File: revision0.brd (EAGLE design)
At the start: 99.5 x 80 mm, 102 parts, among them IC1 MSP430FR698X(1)80-PIN_PN, IC3 FT232RL

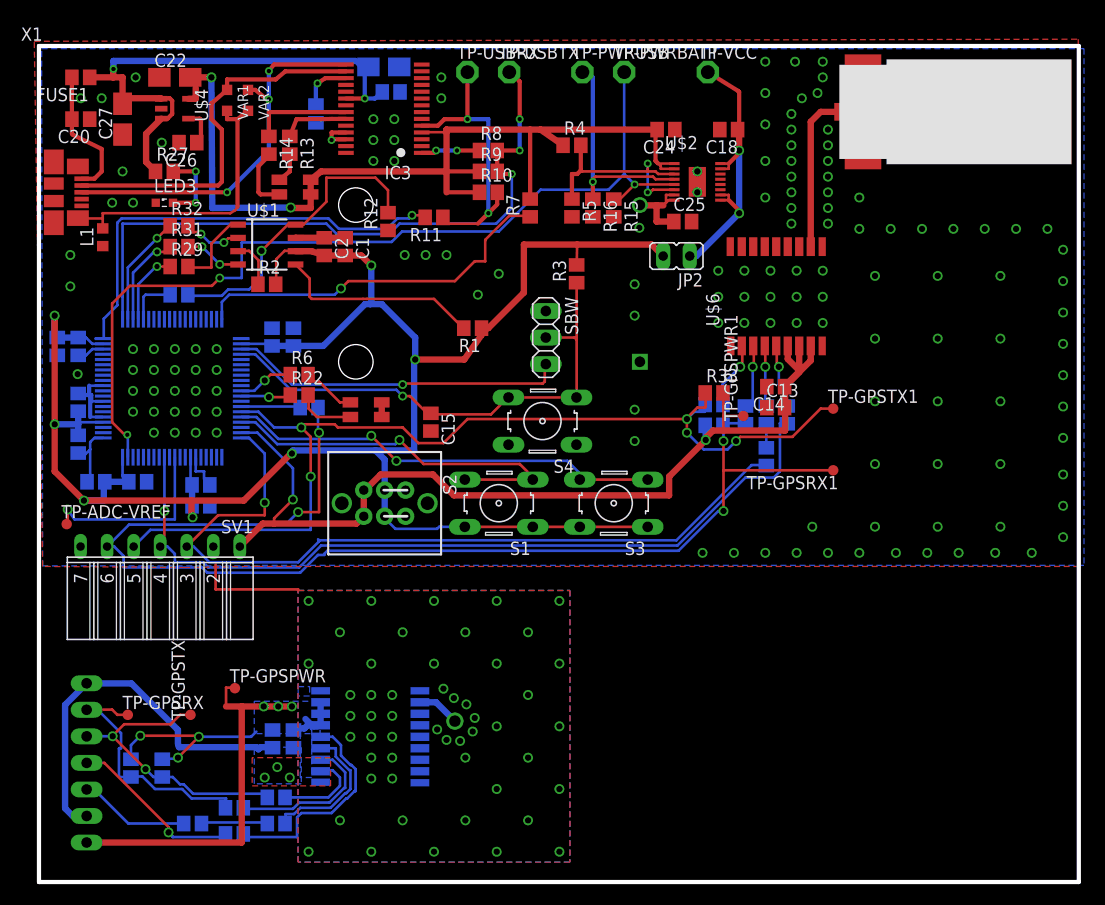
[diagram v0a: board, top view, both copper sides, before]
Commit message: Add ceramic antenna, move the patch antenna connetor a bit
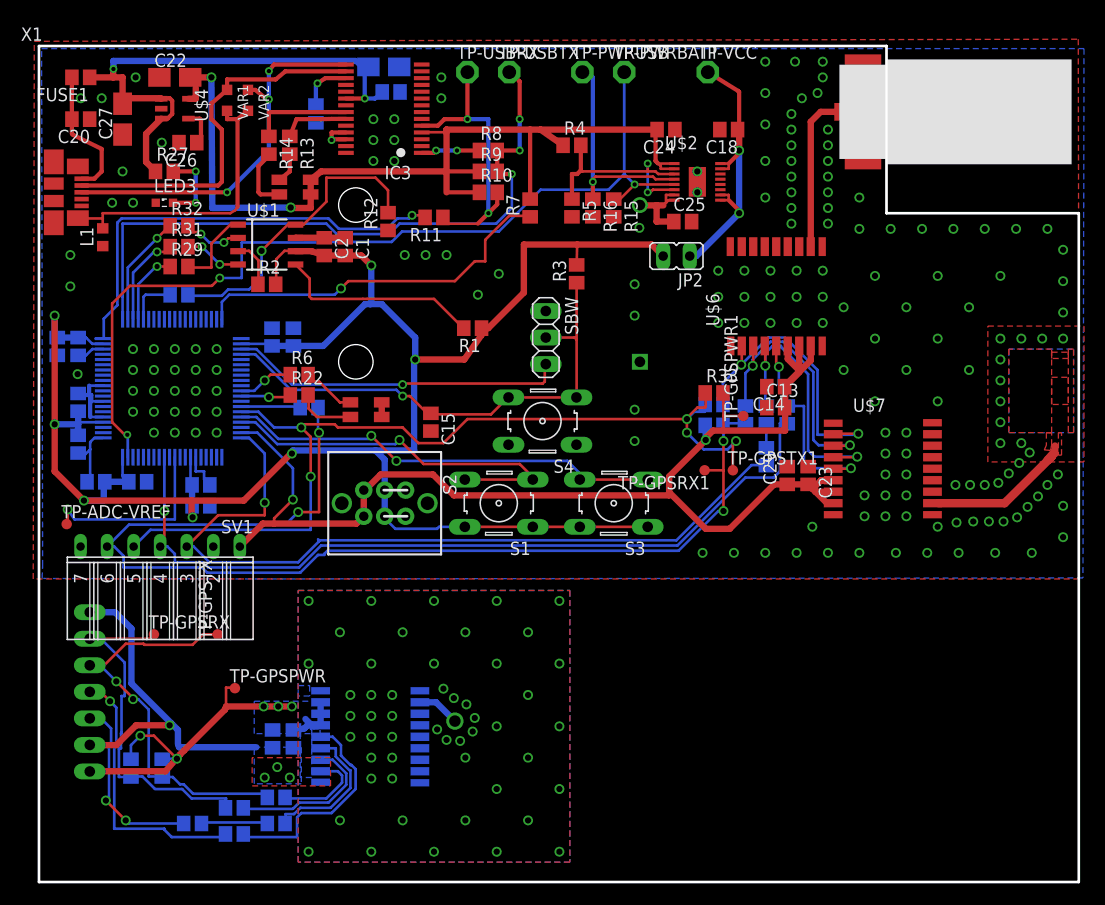
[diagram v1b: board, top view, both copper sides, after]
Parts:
- added C23: 100n, tagps:C0805
- added C29: 1u, tagps:C0805
- added U$7: MAX-8C-0, tagps:MAX-8
- moved TP-GPSRX1 12.3 mm to (63.7, 39.4)
- moved TP-GPSTX1 11.3 mm to (66.4, 39.4)
- moved TP-GPSTX 8.13 mm to (17.1, 23.7)
- moved TP-GPSRX 8.10 mm to (11.0, 23.7)
- moved JP1 6.81 mm to (1.05, 18.2)
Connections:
- removed net N$48: FB4.1, U$6.3
- new net N$15: FB4.1, U$6.3, U$7.3
- net GND: now also C23.1, C29.2, U$7.1, U$7.10, U$7.12
- net MB-PWR_GPS_SENSE: now also C23.2, C29.1, U$7.6, U$7.7, U$7.8
- net N$46: now also U$7.5
- net N$49: now also U$7.2
- net N$50: now also U$7.4
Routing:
- net N$15: track 0.00 -> 26.2 mm, vias 0 -> 2
- net MB-PWR_GPS_SENSE: track 99.1 -> 122.8 mm
- net N$49: track 6.44 -> 28.6 mm, vias 1 -> 2
- net N$50: track 5.89 -> 27.1 mm, vias 1 -> 2
- net PWR_GPS_SENSE: track 59.2 -> 38.3 mm, vias 6 -> 5
- net N$46: track 6.33 -> 20.5 mm, vias 1 -> 2
- net N$31: track 0.00 -> 12.6 mm
- net GND: track 78.9 -> 67.0 mm, vias 194 -> 227
- net GPS-TX: track 28.2 -> 39.9 mm
- net GPS-WAKEUP: track 17.0 -> 26.5 mm
- net GPS-RX: track 24.9 -> 34.2 mm
- net MB-GPS-RX: track 116.0 -> 107.3 mm
- net MB-GPS-TX: track 97.0 -> 89.3 mm
- net GPS-TIMEPULSE: track 10.6 -> 18.1 mm, vias 0 -> 2
- net N$48: track 6.49 -> 0.00 mm, vias 1 -> 0
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- added copper zone on layer 1, net N$20
- added copper zone on layer 1, net N$28
- added copper zone on layer 16, net N$28
- added copper zone on layer 1, net N$29
- added copper zone on layer 1, net N$30
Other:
- outline, holes or cut-outs redrawn
- board text added: "taGPS v2 - antenna test"
- board text removed: "VCCSTAT"

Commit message: Fix gps-power switch scheme
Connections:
- net MB-PWR_GPS_SENSE: now also S2.2.1, S2.2.2; no longer S2.3.1, S2.3.2
- net VCC: now also S2.3.1, S2.3.2; no longer S2.2.1, S2.2.2
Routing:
- net VCC: track 197.3 -> 198.9 mm
- net MB-PWR_GPS_SENSE: track 122.8 -> 124.2 mm
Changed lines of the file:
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@@
 <text x="39.7" y="74.9" size="1.016" layer="100">RX-USB-TX</text>
 <text x="62.6" y="74.9" size="1.016" layer="100">VCC</text>
-<text x="26.6" y="39.9" size="1.016" layer="100" rot="R270">GPS: ON - OFF</text>
+<text x="36.6" y="32.6" size="1.016" layer="100" rot="R180">GPS: ON - OFF</text>
 <text x="47.65" y="32.6" size="1.016" layer="100" rot="R180">CFG GPS</text>
 <text x="61" y="32.6" size="1.016" layer="100" rot="R180">MEM-BATT-STAT</text>
@@
 <wire x1="42.35" y1="52.35" x2="42.35" y2="53" width="0.6096" layer="1"/>
 <wire x1="4.3" y1="36.5" x2="6.2" y2="36.5" width="0.6096" layer="16"/>
-<wire x1="24.3" y1="41.3" x2="32.2" y2="41.3" width="0.6096" layer="16"/>
-<wire x1="32.2" y1="41.3" x2="35.9" y2="41.3" width="0.6096" layer="16"/>
+<wire x1="24.3" y1="41.3" x2="31.2" y2="41.3" width="0.6096" layer="16"/>
+<wire x1="31.2" y1="41.3" x2="35.9" y2="41.3" width="0.6096" layer="16"/>
 <wire x1="35.9" y1="41.3" x2="35.9" y2="49.9" width="0.6096" layer="16"/>
 <wire x1="51.45" y1="59.05" x2="51.5" y2="61" width="0.254" layer="1"/>
@@
 <wire x1="14.7" y1="34.9" x2="14.6" y2="35" width="0.6096" layer="1"/>
 <wire x1="14.6" y1="35" x2="14.6" y2="36.5" width="0.6096" layer="1"/>
-<contactref element="S2" pad="2.1"/>
-<contactref element="S2" pad="2.2"/>
-<wire x1="33.08" y1="37.5" x2="33.08" y2="35" width="0.6096" layer="16"/>
-<wire x1="33.08" y1="37.5" x2="33.08" y2="40.42" width="0.6096" layer="16"/>
-<wire x1="33.08" y1="40.42" x2="32.2" y2="41.3" width="0.6096" layer="16"/>
-<wire x1="34.1" y1="33.8" x2="33.2" y2="34.7" width="0.254" layer="16"/>
-<wire x1="38.1" y1="33.8" x2="34.1" y2="33.8" width="0.254" layer="16"/>
+<wire x1="38.1" y1="33.8" x2="32.28" y2="33.8" width="0.254" layer="16"/>
 <wire x1="38.2894" y1="33.9894" x2="38.1" y2="33.8" width="0.254" layer="16"/>
-<wire x1="33.2" y1="34.7" x2="33.08" y2="35" width="0.254" layer="16"/>
 <wire x1="59.73" y1="59.9" x2="58.63" y2="61" width="0.6096" layer="1"/>
 <wire x1="58.63" y1="61" x2="51.5" y2="61" width="0.6096" layer="1"/>
+<contactref element="S2" pad="3.2"/>
+<contactref element="S2" pad="3.1"/>
+<wire x1="32.28" y1="33.8" x2="31.08" y2="35" width="0.254" layer="16"/>
+<wire x1="31.08" y1="37.5" x2="31.2" y2="37.62" width="0.6096" layer="16"/>
+<wire x1="31.2" y1="37.62" x2="31.2" y2="41.3" width="0.6096" layer="16"/>
+<wire x1="31.08" y1="37.5" x2="31.08" y2="35" width="0.6096" layer="16"/>
 </signal>
 <signal name="GND">
@@
 <via x="12.5" y="15" extent="1-16" drill="0.6"/>
 <wire x1="4.8" y1="25.8" x2="4.86" y2="25.82" width="0.254" layer="1"/>
-<wire x1="3.98" y1="32.1" x2="3.98" y2="26.7" width="0" layer="19" extent="1-16"/>
-<wire x1="3.98" y1="26.7" x2="4.86" y2="25.82" width="0" layer="19" extent="1-16"/>
 <wire x1="97.5" y1="39" x2="97.225" y2="40.95" width="0" layer="19" extent="1-1"/>
+<wire x1="4.86" y1="25.82" x2="3.98" y2="32.1" width="0" layer="19" extent="1-1"/>
 </signal>
 <signal name="GPS-WAKEUP">
@@
 <wire x1="71.65" y1="50.05" x2="71.65" y2="51.3" width="0.6096" layer="1"/>
 <contactref element="SV1" pad="1"/>
-<contactref element="S2" pad="3.2"/>
-<contactref element="S2" pad="3.1"/>
 <contactref element="IC1" pad="39"/>
-<wire x1="30.38" y1="34.3" x2="22.5" y2="34.3" width="0.6096" layer="1"/>
+<wire x1="29.58" y1="34.3" x2="22.5" y2="34.3" width="0.6096" layer="1"/>
 <wire x1="19.35" y1="43" x2="20.9" y2="43" width="0.254" layer="16"/>
 <wire x1="20.9" y1="43" x2="24.3" y2="39.6" width="0.254" layer="16"/>
@@
 <wire x1="21.42" y1="34.3" x2="22.5" y2="34.3" width="0.6096" layer="1"/>
 <wire x1="21.42" y1="34.3" x2="19.22" y2="32.1" width="0.6096" layer="1"/>
-<wire x1="30.38" y1="34.3" x2="31.08" y2="35" width="0.6096" layer="1"/>
-<wire x1="31.08" y1="35" x2="31.08" y2="37.5" width="0.6096" layer="1"/>
 <wire x1="63.8" y1="42.3" x2="63.8" y2="43.7" width="0.6096" layer="16"/>
 <wire x1="60.3" y1="38.8" x2="63.8" y2="42.3" width="0.6096" layer="1"/>
@@
 <wire x1="39.7" y1="37" x2="60.3" y2="37" width="0.6096" layer="1"/>
 <wire x1="37.7" y1="39" x2="39.7" y2="37" width="0.6096" layer="1"/>
-<wire x1="32.7" y1="39" x2="37.7" y2="39" width="0.6096" layer="1"/>
-<wire x1="31.5" y1="37.8" x2="32.7" y2="39" width="0.6096" layer="1"/>
-<wire x1="31.2" y1="37.8" x2="31.5" y2="37.8" width="0.6096" layer="1"/>
 <wire x1="63.8" y1="43.7" x2="63.75" y2="43.7" width="0.6096" layer="16"/>
-<wire x1="31.2" y1="37.8" x2="31.08" y2="37.5" width="0.6096" layer="1"/>
 <via x="63.8" y="42.3" extent="1-16" drill="0.6"/>
 <wire x1="71.4" y1="43.2" x2="71.4" y2="45.4" width="0.6096" layer="1"/>
@@
 <wire x1="76" y1="36.25" x2="75.4" y2="36.25" width="0.6096" layer="1"/>
 <wire x1="75.4" y1="36.25" x2="74.3" y2="37.35" width="0.6096" layer="1"/>
+<contactref element="S2" pad="2.2"/>
+<contactref element="S2" pad="2.1"/>
+<wire x1="33.4" y1="37.5" x2="33.08" y2="37.5" width="0.6096" layer="1"/>
+<wire x1="33.5" y1="37.6" x2="33.4" y2="37.5" width="0.6096" layer="1"/>
+<wire x1="33.5" y1="39" x2="33.5" y2="37.6" width="0.6096" layer="1"/>
+<wire x1="37.7" y1="39" x2="33.5" y2="39" width="0.6096" layer="1"/>
+<wire x1="33.08" y1="37.5" x2="33.08" y2="35" width="0.6096" layer="1"/>
+<wire x1="32.1" y1="33.8" x2="33" y2="34.7" width="0.6096" layer="1"/>
+<wire x1="31.8" y1="33.8" x2="32.1" y2="33.8" width="0.6096" layer="1"/>
+<wire x1="31.7" y1="33.7" x2="31.8" y2="33.8" width="0.6096" layer="1"/>
+<wire x1="30.5" y1="33.7" x2="31.7" y2="33.7" width="0.6096" layer="1"/>
+<wire x1="30.2" y1="34" x2="30.5" y2="33.7" width="0.6096" layer="1"/>
+<wire x1="29.7" y1="34" x2="30.2" y2="34" width="0.6096" layer="1"/>
+<wire x1="33" y1="34.7" x2="33.08" y2="35" width="0.6096" layer="1"/>
+<wire x1="29.7" y1="34" x2="29.58" y2="34.3" width="0.6096" layer="1"/>
 </signal>
 <signal name="N$27" class="1">

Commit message: More PCB board tuning
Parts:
- moved TP-GPSPWR1 10.4 mm to (73.8, 52.9)
- moved R15 10.4 mm to (51.5, 74.3), flipped to the bottom, turned to 90 degrees
- moved R16 9.80 mm to (53.2, 74.3), flipped to the bottom, turned to 90 degrees
- moved C13 8.96 mm to (70.2, 54.4)
- moved C14 8.61 mm to (70.2, 56.0)
- moved U$6 7.32 mm to (65.0, 68.2)
- moved C18 6.74 mm to (60.9, 67.6)
- moved TP-PWRBATT 6.30 mm to (49.7, 77.5)
- moved C25 6.29 mm to (57.1, 67.6)
- moved U$2 6.02 mm to (59.0, 71.5)
- moved TP-PWRUSB 5.40 mm to (57.4, 77.5)
- moved TP-GPSTX1 5.12 mm to (61.8, 41.5)
- moved JP2 4.72 mm to (57.0, 57.4)
- moved C24 4.39 mm to (56.7, 74.9)
- moved R5 4.20 mm to (50.1, 60.4)
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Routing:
- net N$46: track 20.5 -> 38.1 mm
- net N$15: track 26.2 -> 37.7 mm
- net N$50: track 27.1 -> 38.6 mm
- net N$25: track 21.0 -> 11.9 mm
- net VCC: track 198.9 -> 190.3 mm
- net MB-GPS-RX: track 107.3 -> 115.0 mm
- net MB-GPS-TX: track 89.3 -> 81.8 mm, vias 5 -> 4
- net N$27: track 16.3 -> 9.25 mm
- net N$49: track 28.6 -> 35.4 mm
- net MB-PWR_GPS_SENSE: track 124.2 -> 129.3 mm, vias 2 -> 1
- net ADC-BATT: track 89.3 -> 84.7 mm
- net VCCUSB: track 94.7 -> 90.2 mm
- net SBW-TDO/TDI: track 49.2 -> 46.4 mm
- net N$53: track 2.33 -> 0.00 mm
- net N$54: track 1.30 -> 0.00 mm
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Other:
- board text added: "BATT-PWR-USB"
- board text removed: "USB-PWR-BATT"

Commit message: fix power-switcher voltage divider resistor value
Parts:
- R5: value 21.5k -> 39.2k
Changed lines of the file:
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@@
 <attribute name="SPICEPREFIX" value="R" x="48.8" y="69" size="1.778" layer="27" rot="R270" display="off"/>
 </element>
-<element name="R5" library="tagps" package="R0805" value="21.5k" x="50.1" y="60.4" rot="R270">
+<element name="R5" library="tagps" package="R0805" value="39.2k" x="50.1" y="60.4" rot="R270">
 <attribute name="SPICEPREFIX" value="R" x="50.1" y="60.4" size="1.778" layer="27" rot="R270" display="off"/>
 </element>
